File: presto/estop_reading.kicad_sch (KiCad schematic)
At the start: 0 parts

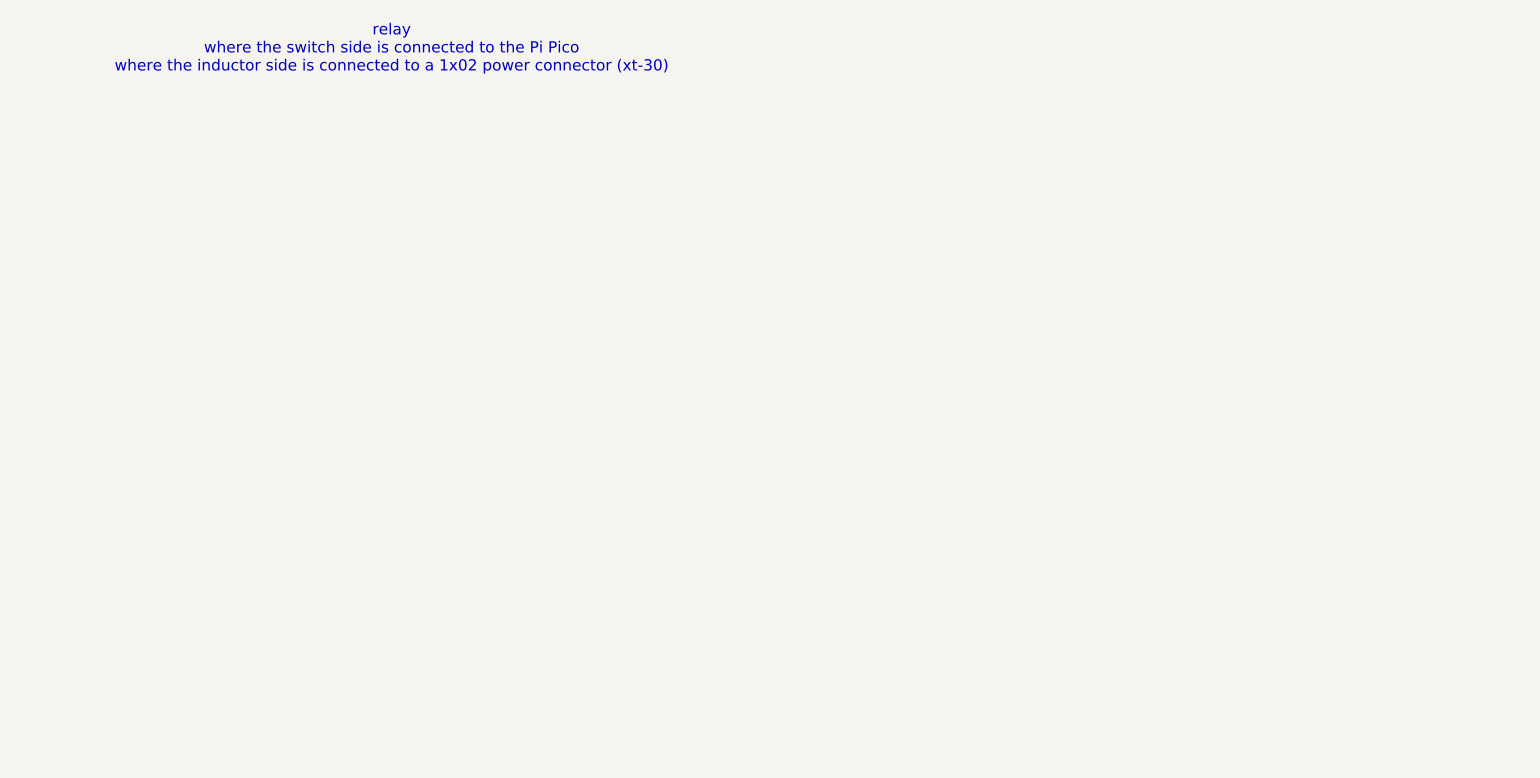
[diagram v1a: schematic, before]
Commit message: Added estop, power, led schematics
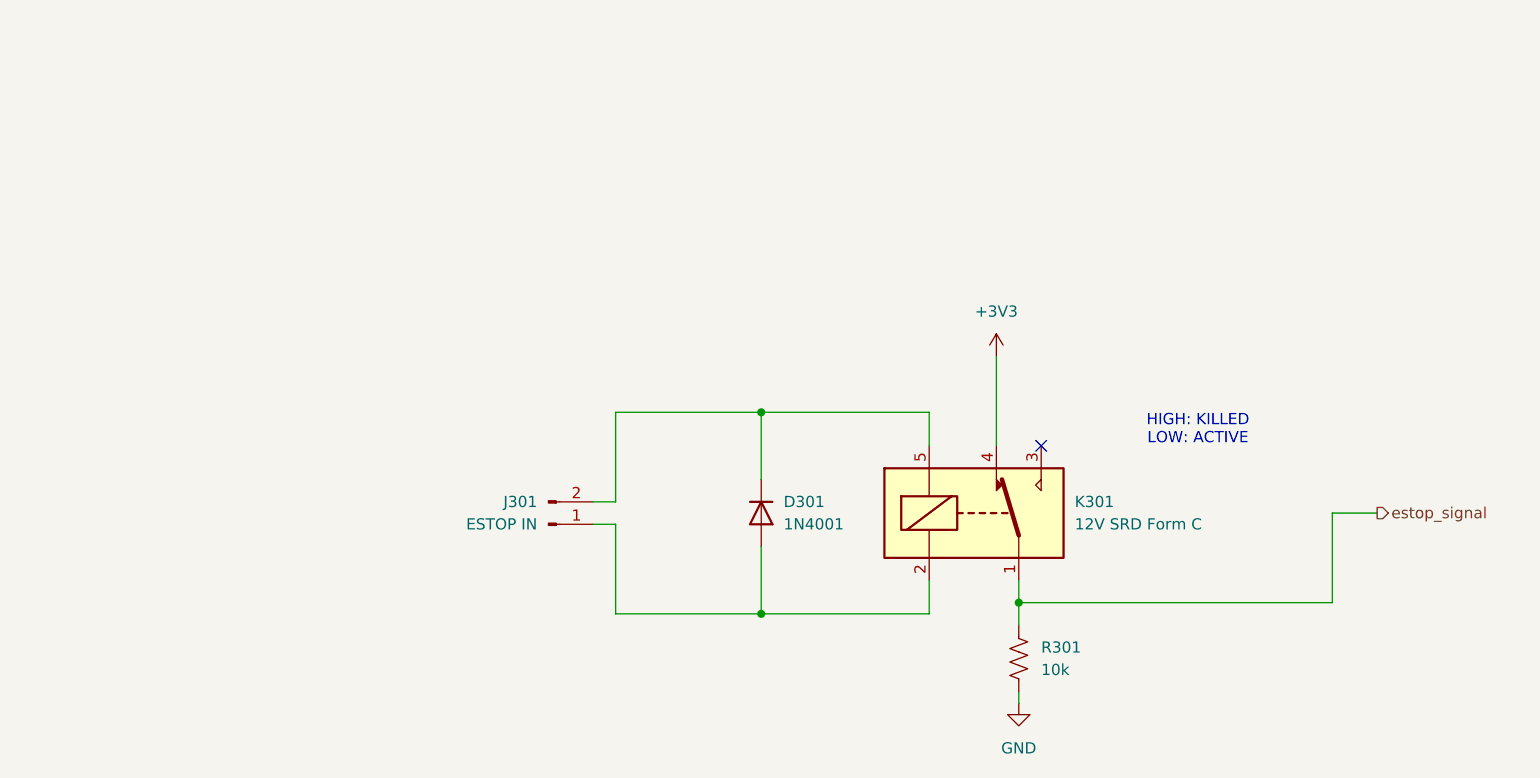
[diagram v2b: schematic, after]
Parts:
- added D301: 1N4001, Diode_THT:D_DO-41_SOD81_P10.16mm_Horizontal, symbol Diode:1N4001
- added J301: ESTOP IN, Connector_AMASS:AMASS_XT30PW-M_1x02_P2.50mm_Horizontal, symbol Connector:Conn_01x02_Pin
- added K301: 12V SRD Form C, Relay_THT:Relay_SPDT_SANYOU_SRD_Series_Form_C, symbol Relay:SANYOU_SRD_Form_C
- added R301: 10k, Resistor_THT:R_Axial_DIN0207_L6.3mm_D2.5mm_P10.16mm_Horizontal, symbol Device:R_US
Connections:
- new net: D301.1 (K), J301.2 (Pin_2), K301.5
- new net: D301.2 (A), J301.1 (Pin_1), K301.2
- new net +3V3: K301.4
- new net GND: R301.2
- new net estop_signal: K301.1, R301.1
- no-connect marks 0 -> 1
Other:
- note added: "HIGH: KILLED LOW: ACTIVE"
- note removed: "relay where the switch side is connected to the Pi Pico where the inductor side is connected to a 1x02 power connector (xt-30)"
